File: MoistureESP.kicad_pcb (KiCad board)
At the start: 2 copper layers, 95 parts, among them J1 Conn_01x03_Pin, J2 Conn_MoisturePCB, J3 Conn_DS18B20, J4 USB4110-GF-A, Q1 SSM6K513NU-LF, Q2 SSM6K513NU-LF, Q3 2N7002W, Q6 RUM002N05T2L, Q7 RUM002N05T2L, Q8 RUM002N05T2L, Q9 RUM002N05T2L, SW1 147873-1, U1 BQ28Z620DRZR, U2 ESP32-WROOM-32D, U3 TPS7A2601DRVR, U4 TPS7A2601DRVR, U5 MAX77757JEFG420+

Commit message: Fix wrong wiring, add pcb design.
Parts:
- removed TP1: TestPoint, TestPoint:TestPoint_Pad_D1.5mm
- added C27: 100nF, Capacitor_SMD:C_0603_1608Metric_Pad1.08x0.95mm_HandSolder, F.Cu at (261.1, 63.1)
- added C8: 100nF, Capacitor_SMD:C_0603_1608Metric_Pad1.08x0.95mm_HandSolder, F.Cu at (261.1, 60.6)
- added D7: SM6T6V8A, Diode_SMD:D_SMB, F.Cu at (263.1, 54.6)
- added D8: BZT52H-B5V1, Diode_SMD:D_SOD-123F, F.Cu at (254.2, 47.9)
- added Q10: DMP3068L-7, Package_TO_SOT_SMD:SOT-23, F.Cu at (248.9, 57.4)
- added Q4: BC817W, Package_TO_SOT_SMD:SOT-323_SC-70, F.Cu at (269.2, 47.9)
- added Q5: BC817W, Package_TO_SOT_SMD:SOT-323_SC-70, F.Cu at (269.2, 51.3)
- added R13: 10K, Resistor_SMD:R_0603_1608Metric_Pad0.98x0.95mm_HandSolder, F.Cu at (253.6, 50.8)
- D6: value BZT52H-B18 -> SM6T6V8A; footprint Diode_SMD:D_SOD-123F -> Diode_SMD:D_SMB
- Q8, Q9: value RUM002N05T2L -> DMP3068L-7; footprint Package_TO_SOT_SMD:SOT-723 -> Package_TO_SOT_SMD:SOT-23
- R41: value 330R -> 10K
- moved D6 202.4 mm to (263.1, 49.0)
- moved R41 176.8 mm to (253.6, 53.3)
- moved Q8 167.9 mm to (248.9, 48.5)
- moved Q9 167.8 mm to (248.9, 52.9)
- moved C16 119.6 mm to (172.1, 91.3)
- moved J4 119.6 mm to (194.0, 83.9)
- moved L1 119.6 mm to (202.4, 96.1)
- moved Q6 119.6 mm to (166.5, 101.5)
- moved Q7 119.6 mm to (166.5, 104.3)
- moved R25 119.6 mm to (162.9, 91.3)
- moved R26 119.6 mm to (162.9, 93.8)
- moved R27 119.6 mm to (162.9, 96.3)
- moved R28 119.6 mm to (162.9, 98.8)
- moved R29 119.6 mm to (172.1, 93.8)
- moved R30 119.6 mm to (172.1, 96.3)
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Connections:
- C11 pad 1: Net-(Q8-D) -> Net-(Q4-C)
- C16 pad 1: GNDA -> GNDD
- D1 pad 2: GNDA -> GNDD
- D2 pad 2: GNDA -> GNDD
- D5 pad 1: Net-(D5-K) -> /mcu/~{CHG_INOK_PROT}
- D6 pad 1: Vsys -> /mcu/BATT_I2C.SDA
- D6 pad 2: GNDPWR -> GNDD
- J2 pad 1: GNDA -> GNDD
- J3 pad 1: GNDA -> GNDD
- Q8 pad 1: Net-(Q8-G) -> GNDPWR
- Q8 pad 2: /mcu/MCU.RTS -> Net-(Q10-S)
- Q8 pad 3: Net-(Q8-D) -> /auxchgr_prot/Vin+
- Q9 pad 1: Net-(Q9-G) -> Net-(Q10-D)
- Q9 pad 2: /mcu/MCU.DTR -> Net-(Q10-S)
- Q9 pad 3: /mcu/BOOT -> /charger/VBat
- R14 pad 1: Net-(Q8-D) -> Net-(Q4-C)
- R19 pad 1: Net-(Q8-G) -> Net-(Q4-B)
- R20 pad 1: Net-(Q9-G) -> Net-(Q5-B)
- R30 pad 1: GNDA -> GNDD
- R41 pad 1: /mcu/~{CHG_INOK_PROT} -> Net-(D8-K)
- R41 pad 2: Net-(D5-K) -> Net-(Q10-S)
- U2 pad 3: Net-(Q8-D) -> Net-(Q4-C)

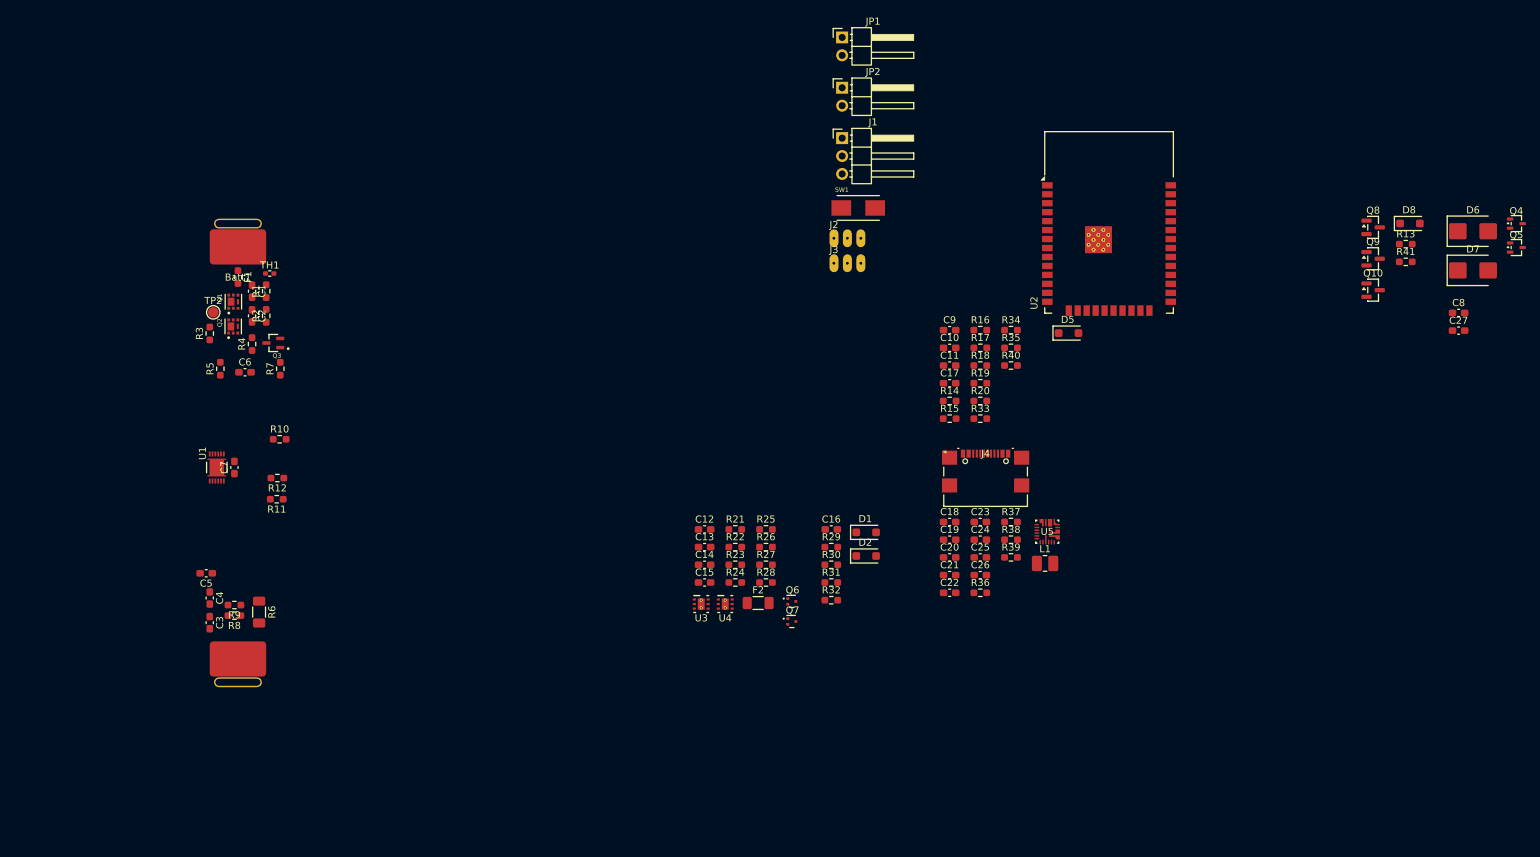
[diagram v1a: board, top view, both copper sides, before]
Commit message: Add footprint to debug connector.
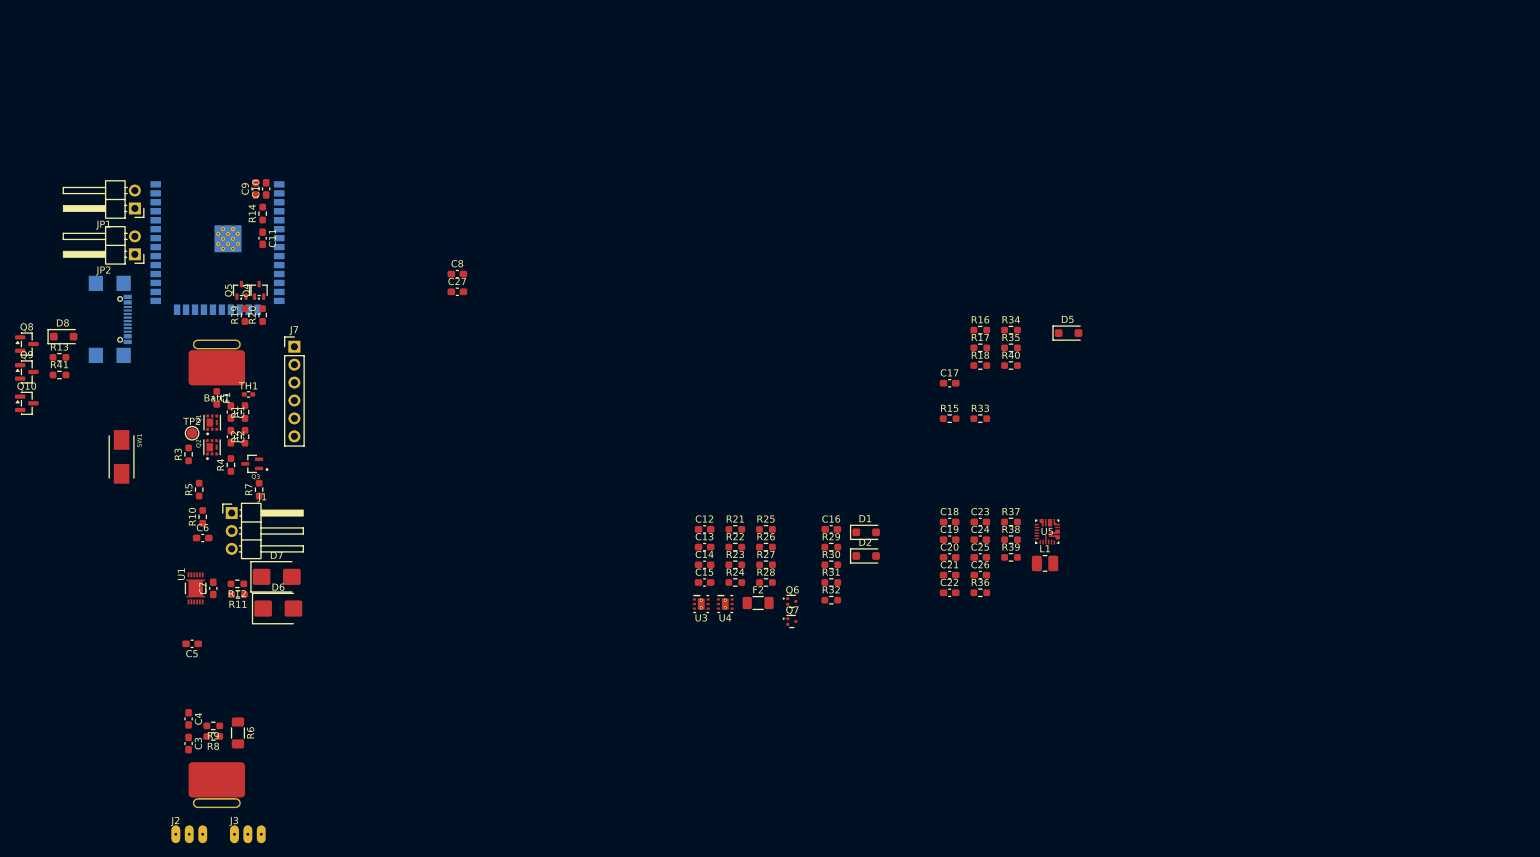
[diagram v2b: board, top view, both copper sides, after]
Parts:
- added J7: Conn_01x06_Pin, Connector_PinHeader_2.54mm:PinHeader_1x06_P2.54mm_Vertical, F.Cu at (96.0, 65.4)
- J4, U2: moved to B.Cu
- moved Q8 191.6 mm to (58.1, 65.0)
- moved D8 191.6 mm to (63.3, 64.0)
- moved Q10 191.6 mm to (58.1, 73.4)
- moved Q9 191.6 mm to (58.1, 69.0)
- moved R41 191.6 mm to (62.7, 69.4)
- moved R13 191.6 mm to (62.7, 66.9)
- moved Q5 180.9 mm to (88.5, 57.4), turned to 90 degrees
- moved Q4 178.5 mm to (91.0, 57.4), turned to 90 degrees
- moved D6 177.6 mm to (93.7, 102.5)
- moved D7 175.1 mm to (93.5, 98.0)
- moved C27 142.1 mm to (119.1, 57.6)
- moved C8 142.1 mm to (119.1, 55.1)
- moved J4 127.0 mm to (69.0, 61.5), turned to 90 degrees
- moved U2 126.4 mm to (85.1, 50.6), turned to 180 degrees
- moved J2 125.9 mm to (79.2, 134.5)
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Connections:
- C13 pad 2: GNDD -> /power/Vdd
- D6 pad 1: /mcu/BATT_I2C.SDA -> /battery/comm.SCL
- D7 pad 1: /mcu/BATT_I2C.SCL -> /battery/comm.SDA
- JP1 pad 1: GNDD -> /power/Vdd
- R21 pad 2: GNDD -> /power/Vdd
- U3 pad 1: GNDD -> /power/Vdd

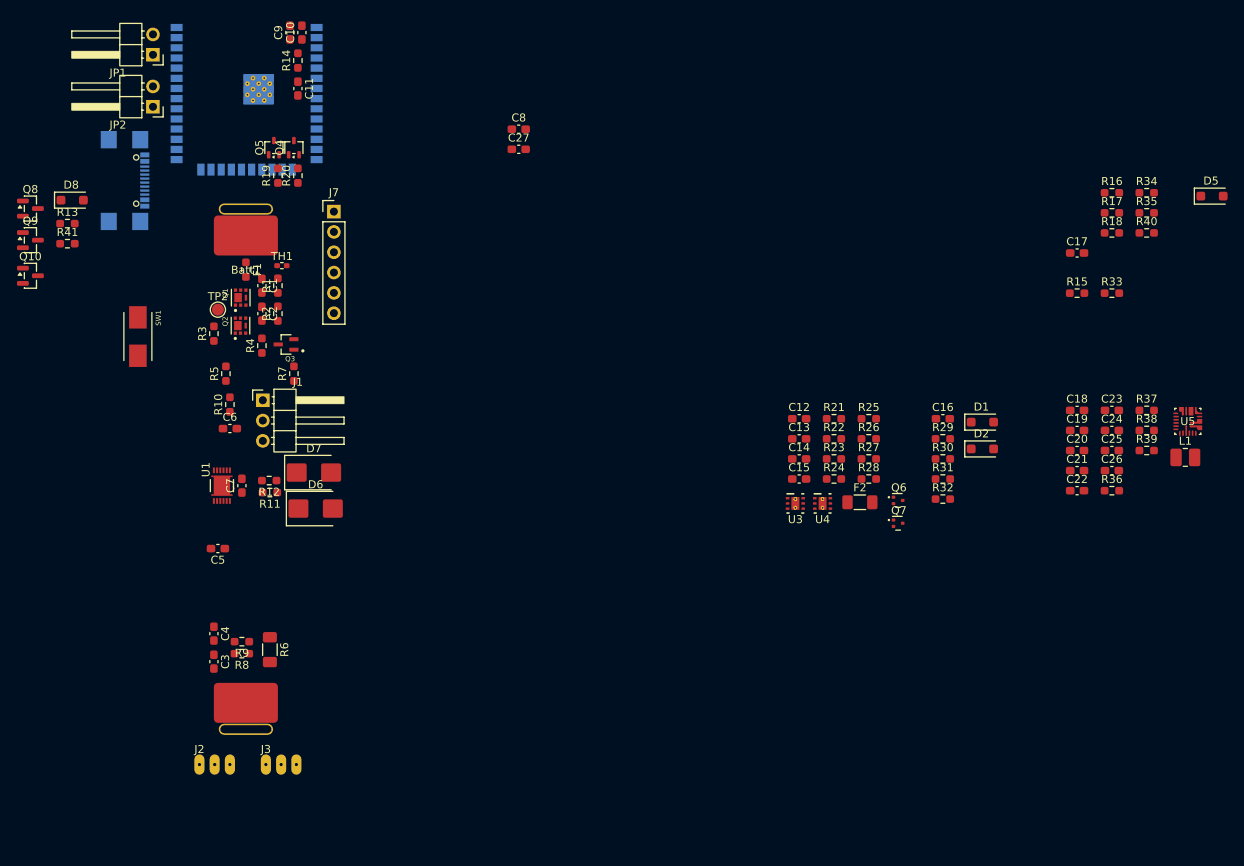
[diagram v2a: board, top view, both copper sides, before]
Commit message: Start placement
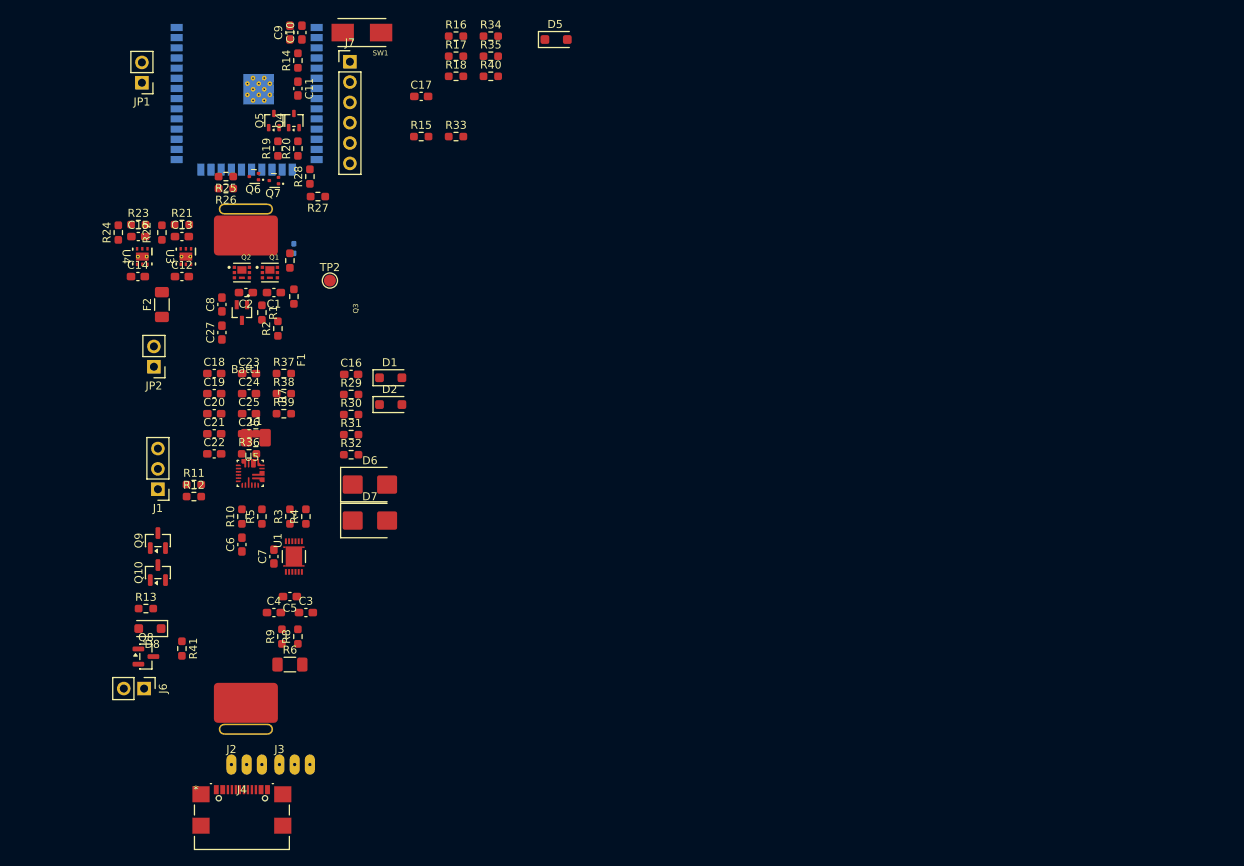
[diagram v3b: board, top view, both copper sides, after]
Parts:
- added J6: Conn_01x02_Pin, Connector_PinHeader_2.54mm:PinHeader_1x02_P2.54mm_Vertical, F.Cu at (72.3, 125.0)
- J1: footprint Connector_PinHeader_2.54mm:PinHeader_1x03_P2.54mm_Horizontal -> Connector_PinHeader_2.54mm:PinHeader_1x03_P2.54mm_Vertical
- J4: moved to F.Cu
- JP1, JP2: footprint Connector_PinHeader_2.54mm:PinHeader_1x02_P2.54mm_Horizontal -> Connector_PinHeader_2.54mm:PinHeader_1x02_P2.54mm_Vertical
- TH1: moved to B.Cu
- moved U5 117.4 mm to (85.5, 98.1)
- moved L1 116.2 mm to (86.2, 93.6)
- moved C18 108.0 mm to (81.0, 85.6)
- moved C19 108.0 mm to (81.0, 88.1)
- moved C20 108.0 mm to (81.0, 90.6)
- moved C21 108.0 mm to (81.0, 93.2)
- moved C22 108.0 mm to (81.0, 95.7)
- moved C23 108.0 mm to (85.4, 85.6)
- moved C24 108.0 mm to (85.4, 88.1)
- moved C25 108.0 mm to (85.4, 90.6)
- moved C26 108.0 mm to (85.4, 93.2)
- moved R36 108.0 mm to (85.4, 95.7)
- moved R37 108.0 mm to (89.7, 85.6)
- moved R38 108.0 mm to (89.7, 88.1)
- moved R39 108.0 mm to (89.7, 90.6)
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
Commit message: Add someplacement.
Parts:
- C17, D5, JP1, R33, R34, R35, R40, SW1: moved to B.Cu
- U2: value ESP32-WROOM-32D -> ESP32-WROOM-32; footprint RF_Module:ESP32-WROOM-32D -> RF_Module:ESP32-WROOM-32
- moved D5 55.3 mm to (72.5, 64.5), turned to 180 degrees
- moved R35 48.8 mm to (74.0, 71.5), turned to -90 degrees
- moved R40 46.3 mm to (73.0, 66.5), turned to 180 degrees
- moved R34 45.0 mm to (71.0, 49.5), turned to -90 degrees
- moved R33 40.4 mm to (71.0, 52.9), turned to -90 degrees
- moved C17 33.4 mm to (73.5, 52.0)
- moved R18 33.2 mm to (79.5, 58.0), turned to 90 degrees
- moved R16 31.7 mm to (80.5, 51.0)
- moved R17 31.6 mm to (80.5, 53.0)
- moved SW1 31.0 mm to (73.0, 59.0), turned to 90 degrees
- moved R15 26.0 mm to (81.0, 58.0), turned to 90 degrees
- moved JP1 2.92 mm to (73.5, 46.8), turned to 0 degrees
- moved J7 1.92 mm to (97.5, 48.5)
- moved Q4 1.50 mm to (92.5, 54.0)
- moved Q5 1.50 mm to (90.0, 54.0)
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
